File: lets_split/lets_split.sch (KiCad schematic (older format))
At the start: 60 parts, among them J1 3PIN, J2 6PIN, J3 3PIN, SW1 SW_PUSH, SW10 SW_PUSH, SW11 SW_PUSH, SW12 SW_PUSH, SW13 SW_PUSH, SW14 SW_PUSH, SW15 SW_PUSH, SW16 SW_PUSH, SW17 SW_PUSH, SW18 SW_PUSH, SW19 SW_PUSH, SW2 SW_PUSH, SW20 SW_PUSH, SW21 SW_PUSH, SW22 SW_PUSH, SW23 SW_PUSH, SW24 SW_PUSH, SW3 SW_PUSH, SW4 SW_PUSH, SW5 SW_PUSH, SW6 SW_PUSH, SW7 SW_PUSH, SW8 SW_PUSH, SW9 SW_PUSH, U1 TEENSY2.0, U2 HOLE, U3 HOLE, U4 HOLE, U5 HOLE

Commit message: Replace diode modules with SMD compatible one
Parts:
- D1, D10, D11, D12, D13, D14, D15, D16, D17, D18, D19, D2, D20, D21, D22, D23, D24, D3, D4, D5, D6, D7, D8, D9: footprint Diodes_ThroughHole:Diode_DO-41_SOD81_Horizontal_RM10 -> local:Diode_TH_SOD123
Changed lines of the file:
@@
 EESchema Schematic File Version 2
-LIBS:power
-LIBS:device
-LIBS:transistors
-LIBS:conn
-LIBS:linear
-LIBS:regul
-LIBS:74xx
-LIBS:cmos4000
-LIBS:adc-dac
-LIBS:memory
-LIBS:xilinx
-LIBS:microcontrollers
-LIBS:dsp
-LIBS:microchip
-LIBS:analog_switches
-LIBS:motorola
-LIBS:texas
-LIBS:intel
-LIBS:audio
-LIBS:interface
-LIBS:digital-audio
-LIBS:philips
-LIBS:display
-LIBS:cypress
-LIBS:siliconi
-LIBS:opto
-LIBS:atmel
-LIBS:contrib
-LIBS:valves
-LIBS:component
 LIBS:lets_split-cache
-EELAYER 25 0
+EELAYER 26 0
 EELAYER END
 $Descr A4 11693 8268
@@
 F 0 "D1" H 5750 2450 50  0000 C CNN
 F 1 "D" H 5750 2250 50  0000 C CNN
-F 2 "Diodes_ThroughHole:Diode_DO-41_SOD81_Horizontal_RM10" H 5750 2350 50  0001 C CNN
+F 2 "local:Diode_TH_SOD123" H 5750 2350 50  0001 C CNN
 F 3 "" H 5750 2350 50  0000 C CNN
 	1    5750 2350
@@
 F 0 "D5" H 6500 2450 50  0000 C CNN
 F 1 "D" H 6500 2250 50  0000 C CNN
-F 2 "Diodes_ThroughHole:Diode_DO-41_SOD81_Horizontal_RM10" H 6500 2350 50  0001 C CNN
+F 2 "local:Diode_TH_SOD123" H 6500 2350 50  0001 C CNN
 F 3 "" H 6500 2350 50  0000 C CNN
 	1    6500 2350
@@
 F 0 "D9" H 7200 2450 50  0000 C CNN
 F 1 "D" H 7200 2250 50  0000 C CNN
-F 2 "Diodes_ThroughHole:Diode_DO-41_SOD81_Horizontal_RM10" H 7200 2350 50  0001 C CNN
+F 2 "local:Diode_TH_SOD123" H 7200 2350 50  0001 C CNN
 F 3 "" H 7200 2350 50  0000 C CNN
 	1    7200 2350
@@
 F 0 "D13" H 7950 2450 50  0000 C CNN
 F 1 "D" H 7950 2250 50  0000 C CNN
-F 2 "Diodes_ThroughHole:Diode_DO-41_SOD81_Horizontal_RM10" H 7950 2350 50  0001 C CNN
+F 2 "local:Diode_TH_SOD123" H 7950 2350 50  0001 C CNN
 F 3 "" H 7950 2350 50  0000 C CNN
 	1    7950 2350
@@
 F 0 "D17" H 8700 2450 50  0000 C CNN
 F 1 "D" H 8700 2250 50  0000 C CNN
-F 2 "Diodes_ThroughHole:Diode_DO-41_SOD81_Horizontal_RM10" H 8700 2350 50  0001 C CNN
+F 2 "local:Diode_TH_SOD123" H 8700 2350 50  0001 C CNN
 F 3 "" H 8700 2350 50  0000 C CNN
 	1    8700 2350
@@
 F 0 "D21" H 9450 2450 50  0000 C CNN
 F 1 "D" H 9450 2250 50  0000 C CNN
-F 2 "Diodes_ThroughHole:Diode_DO-41_SOD81_Horizontal_RM10" H 9450 2350 50  0001 C CNN
+F 2 "local:Diode_TH_SOD123" H 9450 2350 50  0001 C CNN
 F 3 "" H 9450 2350 50  0000 C CNN
 	1    9450 2350
@@
 F 0 "D2" H 5750 2950 50  0000 C CNN
 F 1 "D" H 5750 2750 50  0000 C CNN
-F 2 "Diodes_ThroughHole:Diode_DO-41_SOD81_Horizontal_RM10" H 5750 2850 50  0001 C CNN
+F 2 "local:Diode_TH_SOD123" H 5750 2850 50  0001 C CNN
 F 3 "" H 5750 2850 50  0000 C CNN
 	1    5750 2850
@@
 F 0 "D6" H 6500 2950 50  0000 C CNN
 F 1 "D" H 6500 2750 50  0000 C CNN
-F 2 "Diodes_ThroughHole:Diode_DO-41_SOD81_Horizontal_RM10" H 6500 2850 50  0001 C CNN
+F 2 "local:Diode_TH_SOD123" H 6500 2850 50  0001 C CNN
 F 3 "" H 6500 2850 50  0000 C CNN
 	1    6500 2850
@@
 F 0 "D10" H 7200 2950 50  0000 C CNN
 F 1 "D" H 7200 2750 50  0000 C CNN
-F 2 "Diodes_ThroughHole:Diode_DO-41_SOD81_Horizontal_RM10" H 7200 2850 50  0001 C CNN
+F 2 "local:Diode_TH_SOD123" H 7200 2850 50  0001 C CNN
 F 3 "" H 7200 2850 50  0000 C CNN
 	1    7200 2850
@@
 F 0 "D14" H 7950 2950 50  0000 C CNN
 F 1 "D" H 7950 2750 50  0000 C CNN
-F 2 "Diodes_ThroughHole:Diode_DO-41_SOD81_Horizontal_RM10" H 7950 2850 50  0001 C CNN
+F 2 "local:Diode_TH_SOD123" H 7950 2850 50  0001 C CNN
 F 3 "" H 7950 2850 50  0000 C CNN
 	1    7950 2850
@@
 F 0 "D18" H 8700 2950 50  0000 C CNN
 F 1 "D" H 8700 2750 50  0000 C CNN
-F 2 "Diodes_ThroughHole:Diode_DO-41_SOD81_Horizontal_RM10" H 8700 2850 50  0001 C CNN
+F 2 "local:Diode_TH_SOD123" H 8700 2850 50  0001 C CNN
 F 3 "" H 8700 2850 50  0000 C CNN
 	1    8700 2850
@@
 F 0 "D22" H 9450 2950 50  0000 C CNN
 F 1 "D" H 9450 2750 50  0000 C CNN
-F 2 "Diodes_ThroughHole:Diode_DO-41_SOD81_Horizontal_RM10" H 9450 2850 50  0001 C CNN
+F 2 "local:Diode_TH_SOD123" H 9450 2850 50  0001 C CNN
 F 3 "" H 9450 2850 50  0000 C CNN
 	1    9450 2850
@@
 F 0 "D3" H 5750 3450 50  0000 C CNN
 F 1 "D" H 5750 3250 50  0000 C CNN
-F 2 "Diodes_ThroughHole:Diode_DO-41_SOD81_Horizontal_RM10" H 5750 3350 50  0001 C CNN
+F 2 "local:Diode_TH_SOD123" H 5750 3350 50  0001 C CNN
 F 3 "" H 5750 3350 50  0000 C CNN
 	1    5750 3350
@@
 F 0 "D7" H 6500 3450 50  0000 C CNN
 F 1 "D" H 6500 3250 50  0000 C CNN
-F 2 "Diodes_ThroughHole:Diode_DO-41_SOD81_Horizontal_RM10" H 6500 3350 50  0001 C CNN
+F 2 "local:Diode_TH_SOD123" H 6500 3350 50  0001 C CNN
 F 3 "" H 6500 3350 50  0000 C CNN
 	1    6500 3350
@@
 F 0 "D11" H 7200 3450 50  0000 C CNN
 F 1 "D" H 7200 3250 50  0000 C CNN
-F 2 "Diodes_ThroughHole:Diode_DO-41_SOD81_Horizontal_RM10" H 7200 3350 50  0001 C CNN
+F 2 "local:Diode_TH_SOD123" H 7200 3350 50  0001 C CNN
 F 3 "" H 7200 3350 50  0000 C CNN
 	1    7200 3350
@@
 F 0 "D15" H 7950 3450 50  0000 C CNN
 F 1 "D" H 7950 3250 50  0000 C CNN
-F 2 "Diodes_ThroughHole:Diode_DO-41_SOD81_Horizontal_RM10" H 7950 3350 50  0001 C CNN
+F 2 "local:Diode_TH_SOD123" H 7950 3350 50  0001 C CNN
 F 3 "" H 7950 3350 50  0000 C CNN
 	1    7950 3350
@@
 F 0 "D19" H 8700 3450 50  0000 C CNN
 F 1 "D" H 8700 3250 50  0000 C CNN
-F 2 "Diodes_ThroughHole:Diode_DO-41_SOD81_Horizontal_RM10" H 8700 3350 50  0001 C CNN
+F 2 "local:Diode_TH_SOD123" H 8700 3350 50  0001 C CNN
 F 3 "" H 8700 3350 50  0000 C CNN
 	1    8700 3350
@@
 F 0 "D23" H 9450 3450 50  0000 C CNN
 F 1 "D" H 9450 3250 50  0000 C CNN
-F 2 "Diodes_ThroughHole:Diode_DO-41_SOD81_Horizontal_RM10" H 9450 3350 50  0001 C CNN
+F 2 "local:Diode_TH_SOD123" H 9450 3350 50  0001 C CNN
 F 3 "" H 9450 3350 50  0000 C CNN
 	1    9450 3350
@@
 F 0 "D4" H 5750 3950 50  0000 C CNN
 F 1 "D" H 5750 3750 50  0000 C CNN
-F 2 "Diodes_ThroughHole:Diode_DO-41_SOD81_Horizontal_RM10" H 5750 3850 50  0001 C CNN
+F 2 "local:Diode_TH_SOD123" H 5750 3850 50  0001 C CNN
 F 3 "" H 5750 3850 50  0000 C CNN
 	1    5750 3850
@@
 F 0 "D8" H 6500 3950 50  0000 C CNN
 F 1 "D" H 6500 3750 50  0000 C CNN
-F 2 "Diodes_ThroughHole:Diode_DO-41_SOD81_Horizontal_RM10" H 6500 3850 50  0001 C CNN
+F 2 "local:Diode_TH_SOD123" H 6500 3850 50  0001 C CNN
 F 3 "" H 6500 3850 50  0000 C CNN
 	1    6500 3850
@@
 F 0 "D12" H 7200 3950 50  0000 C CNN
 F 1 "D" H 7200 3750 50  0000 C CNN
-F 2 "Diodes_ThroughHole:Diode_DO-41_SOD81_Horizontal_RM10" H 7200 3850 50  0001 C CNN
+F 2 "local:Diode_TH_SOD123" H 7200 3850 50  0001 C CNN
 F 3 "" H 7200 3850 50  0000 C CNN
 	1    7200 3850
@@
 F 0 "D16" H 7950 3950 50  0000 C CNN
 F 1 "D" H 7950 3750 50  0000 C CNN
-F 2 "Diodes_ThroughHole:Diode_DO-41_SOD81_Horizontal_RM10" H 7950 3850 50  0001 C CNN
+F 2 "local:Diode_TH_SOD123" H 7950 3850 50  0001 C CNN
 F 3 "" H 7950 3850 50  0000 C CNN
 	1    7950 3850
@@
 F 0 "D20" H 8700 3950 50  0000 C CNN
 F 1 "D" H 8700 3750 50  0000 C CNN
-F 2 "Diodes_ThroughHole:Diode_DO-41_SOD81_Horizontal_RM10" H 8700 3850 50  0001 C CNN
+F 2 "local:Diode_TH_SOD123" H 8700 3850 50  0001 C CNN
 F 3 "" H 8700 3850 50  0000 C CNN
 	1    8700 3850
@@
 F 0 "D24" H 9450 3950 50  0000 C CNN
 F 1 "D" H 9450 3750 50  0000 C CNN
-F 2 "Diodes_ThroughHole:Diode_DO-41_SOD81_Horizontal_RM10" H 9450 3850 50  0001 C CNN
+F 2 "local:Diode_TH_SOD123" H 9450 3850 50  0001 C CNN
 F 3 "" H 9450 3850 50  0000 C CNN
 	1    9450 3850

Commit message: Replace resistor footprint with one having silk on both sides
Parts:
- R1, R2: footprint footprint:RESISTOR -> local:RESISTOR
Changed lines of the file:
@@
 F 0 "R2" V 6380 950 50  0000 C CNN
 F 1 "R" V 6300 950 50  0000 C CNN
-F 2 "footprint:RESISTOR" V 6230 950 50  0001 C CNN
+F 2 "local:RESISTOR" V 6230 950 50  0001 C CNN
 F 3 "" H 6300 950 50  0000 C CNN
 	1    6300 950
@@
 F 0 "R1" V 4680 750 50  0000 C CNN
 F 1 "R" V 4600 750 50  0000 C CNN
-F 2 "footprint:RESISTOR" V 4530 750 50  0001 C CNN
+F 2 "local:RESISTOR" V 4530 750 50  0001 C CNN
 F 3 "" H 4600 750 50  0000 C CNN
 	1    4600 750

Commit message: Replace Teensy 2.0 symbol with Pro Micro one
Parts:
- removed U1: TEENSY2.0, footprint:TEENSY_2.0, symbol TEENSY2.0
- added U1: ProMicro, local:ProMicro, symbol ProMicro
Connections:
- wire segments 24 -> 31
- no-connect marks 0 -> 8
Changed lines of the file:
@@
 EESchema Schematic File Version 2
+LIBS:promicro
 LIBS:lets_split-cache
 EELAYER 26 0
@@
 Connection ~ 8850 3200
 $Comp
-L TEENSY2.0 U1
-U 1 1 57D48AE5
-P 2000 2950
-F 0 "U1" V 2050 2950 60  0000 C CNN
-F 1 "TEENSY2.0" V 1950 2950 60  0000 C CNN
-F 2 "footprint:TEENSY_2.0" H 2000 2950 60  0001 C CNN
-F 3 "" H 2000 2950 60  0000 C CNN
-	1    2000 2950
-	1    0    0    -1
-$EndComp
-$Comp
 L 6PIN J2
 U 1 1 57D49FBD
@@
 Wire Wire Line
 	6400 1150 6400 1450
-Text GLabel 2600 4150 2    60   Input ~ 0
-data
 Text GLabel 6450 950  1    60   Input ~ 0
 data
@@
 	1    4600 600
 	0    1    1    0
-$EndComp
-Wire Wire Line
-	4600 900  4600 4050
-Wire Wire Line
-	4600 4050 2600 4050
-Text GLabel 2600 2750 2    60   Input ~ 0
-col0
-Text GLabel 2600 2850 2    60   Input ~ 0
-col1
-Text GLabel 2600 2950 2    60   Input ~ 0
-col2
-Text GLabel 2600 3050 2    60   Input ~ 0
-col3
-Text GLabel 2600 2500 2    60   Input ~ 0
-col4
-Text GLabel 2600 2600 2    60   Input ~ 0
-col5
-Text GLabel 2600 3350 2    60   Input ~ 0
-row3
-Text GLabel 2600 3450 2    60   Input ~ 0
-row2
-Text GLabel 2600 2050 2    60   Input ~ 0
-row1
-Text GLabel 2600 2150 2    60   Input ~ 0
-row0
-$Comp
-L VCC #PWR07
-U 1 1 57D5E2B3
-P 2600 1850
-F 0 "#PWR07" H 2600 1700 50  0001 C CNN
-F 1 "VCC" H 2600 2000 50  0000 C CNN
-F 2 "" H 2600 1850 50  0000 C CNN
-F 3 "" H 2600 1850 50  0000 C CNN
-	1    2600 1850
-	0    1    1    0
-$EndComp
-$Comp
-L GND #PWR08
-U 1 1 57D5FCCF
-P 2600 1650
-F 0 "#PWR08" H 2600 1400 50  0001 C CNN
-F 1 "GND" H 2600 1500 50  0000 C CNN
-F 2 "" H 2600 1650 50  0000 C CNN
-F 3 "" H 2600 1650 50  0000 C CNN
-	1    2600 1650
-	0    -1   -1   0
-$EndComp
-$Comp
-L GND #PWR09
-U 1 1 57D5FDD2
-P 2600 3850
-F 0 "#PWR09" H 2600 3600 50  0001 C CNN
-F 1 "GND" H 2600 3700 50  0000 C CNN
-F 2 "" H 2600 3850 50  0000 C CNN
-F 3 "" H 2600 3850 50  0000 C CNN
-	1    2600 3850
-	0    -1   -1   0
-$EndComp
-$Comp
-L GND #PWR010
-U 1 1 57D5FE56
-P 2600 3950
-F 0 "#PWR010" H 2600 3700 50  0001 C CNN
-F 1 "GND" H 2600 3800 50  0000 C CNN
-F 2 "" H 2600 3950 50  0000 C CNN
-F 3 "" H 2600 3950 50  0000 C CNN
-	1    2600 3950
-	0    -1   -1   0
 $EndComp
 Text GLabel 5150 2200 1    60   Input ~ 0
@@
 	1    0    0    -1
 $EndComp
+$Comp
+L ProMicro U1
+U 1 1 59A40F45
+P 2850 3150
+F 0 "U1" H 2550 3850 60  0000 C CNN
+F 1 "ProMicro" H 2850 2450 60  0000 C CNN
+F 2 "local:ProMicro" H 2950 2900 60  0001 C CNN
+F 3 "" H 2950 2900 60  0000 C CNN
+	1    2850 3150
+	1    0    0    -1
+$EndComp
+$Comp
+L GND #PWR?
+U 1 1 59A417D7
+P 3500 2700
+F 0 "#PWR?" H 3500 2450 50  0001 C CNN
+F 1 "GND" H 3500 2550 50  0000 C CNN
+F 2 "" H 3500 2700 50  0000 C CNN
+F 3 "" H 3500 2700 50  0000 C CNN
+	1    3500 2700
+	0    -1   -1   0
+$EndComp
+Wire Wire Line
+	3500 2700 3400 2700
+$Comp
+L VCC #PWR?
+U 1 1 59A41DD4
+P 3500 2900
+F 0 "#PWR?" H 3500 2750 50  0001 C CNN
+F 1 "VCC" H 3500 3050 50  0000 C CNN
+F 2 "" H 3500 2900 50  0000 C CNN
+F 3 "" H 3500 2900 50  0000 C CNN
+	1    3500 2900
+	0    1    1    0
+$EndComp
+Wire Wire Line
+	3400 2900 3500 2900
+Text GLabel 2300 3500 0    60   Input ~ 0
+row1
+Text GLabel 2300 3400 0    60   Input ~ 0
+row0
+Text GLabel 2300 3600 0    60   Input ~ 0
+row2
+Text GLabel 2300 3700 0    60   Input ~ 0
+row3
+Text GLabel 3400 3200 2    60   Input ~ 0
+col0
+Text GLabel 3400 3300 2    60   Input ~ 0
+col1
+Text GLabel 3400 3400 2    60   Input ~ 0
+col2
+Text GLabel 3400 3500 2    60   Input ~ 0
+col3
+Text GLabel 3400 3600 2    60   Input ~ 0
+col4
+Text GLabel 3400 3700 2    60   Input ~ 0
+col5
+$Comp
+L GND #PWR?
+U 1 1 59A45F78
+P 2200 2800
+F 0 "#PWR?" H 2200 2550 50  0001 C CNN
+F 1 "GND" H 2200 2650 50  0000 C CNN
+F 2 "" H 2200 2800 50  0000 C CNN
+F 3 "" H 2200 2800 50  0000 C CNN
+	1    2200 2800
+	0    1    1    0
+$EndComp
+Wire Wire Line
+	2300 2800 2200 2800
+Wire Wire Line
+	2300 2900 2250 2900
+Wire Wire Line
+	2250 2900 2250 2800
+Connection ~ 2250 2800
+Text GLabel 2300 3100 0    60   Input ~ 0
+data
+NoConn ~ 2300 2600
+NoConn ~ 2300 2700
+NoConn ~ 2300 3200
+NoConn ~ 2300 3300
+NoConn ~ 3400 2600
+NoConn ~ 3400 2800
+NoConn ~ 3400 3000
+NoConn ~ 3400 3100
+Wire Wire Line
+	1900 3000 2300 3000
+Wire Wire Line
+	4600 900  4600 1750
+Wire Wire Line
+	4600 1750 1900 1750
+Wire Wire Line
+	1900 1750 1900 3000
 $EndSCHEMATC

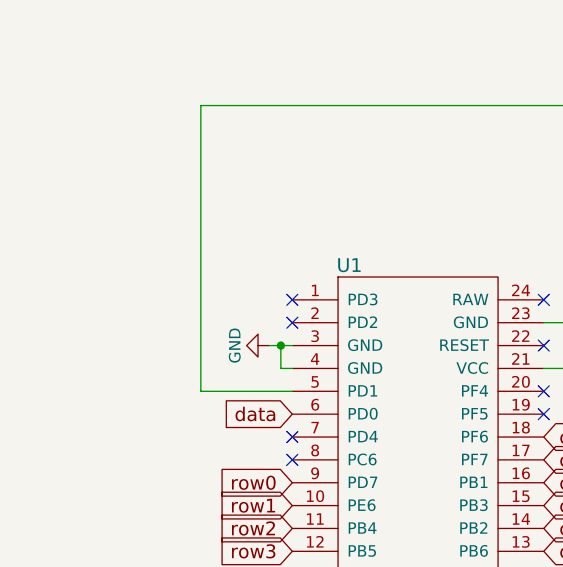
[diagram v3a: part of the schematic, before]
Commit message: Add IO pad for RGB underglow
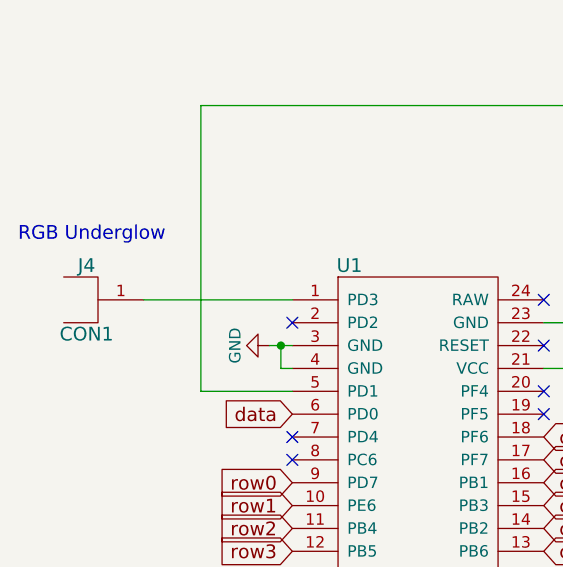
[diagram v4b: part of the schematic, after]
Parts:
- added J4: CON1, local:CON1, symbol CON1
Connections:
- net at U1.1 (PD3): now also J4.1
- no-connect marks 8 -> 7
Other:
- note added: "RGB Underglow"
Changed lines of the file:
@@
 EESchema Schematic File Version 2
 LIBS:promicro
+LIBS:local
 LIBS:lets_split-cache
 EELAYER 26 0
@@
 $EndComp
 $Comp
-L GND #PWR?
+L GND #PWR07
 U 1 1 59A417D7
 P 3500 2700
-F 0 "#PWR?" H 3500 2450 50  0001 C CNN
+F 0 "#PWR07" H 3500 2450 50  0001 C CNN
 F 1 "GND" H 3500 2550 50  0000 C CNN
 F 2 "" H 3500 2700 50  0000 C CNN
@@
 	3500 2700 3400 2700
 $Comp
-L VCC #PWR?
+L VCC #PWR09
 U 1 1 59A41DD4
 P 3500 2900
-F 0 "#PWR?" H 3500 2750 50  0001 C CNN
+F 0 "#PWR09" H 3500 2750 50  0001 C CNN
 F 1 "VCC" H 3500 3050 50  0000 C CNN
 F 2 "" H 3500 2900 50  0000 C CNN
@@
 col5
 $Comp
-L GND #PWR?
+L GND #PWR08
 U 1 1 59A45F78
 P 2200 2800
-F 0 "#PWR?" H 2200 2550 50  0001 C CNN
+F 0 "#PWR08" H 2200 2550 50  0001 C CNN
 F 1 "GND" H 2200 2650 50  0000 C CNN
 F 2 "" H 2200 2800 50  0000 C CNN
@@
 Text GLabel 2300 3100 0    60   Input ~ 0
 data
-NoConn ~ 2300 2600
 NoConn ~ 2300 2700
 NoConn ~ 2300 3200
@@
 Wire Wire Line
 	1900 1750 1900 3000
+$Comp
+L CON1 J4
+U 1 1 59A446B6
+P 1400 2600
+F 0 "J4" H 1400 2750 60  0000 C CNN
+F 1 "CON1" H 1400 2450 60  0000 C CNN
+F 2 "local:CON1" H 1350 2600 60  0001 C CNN
+F 3 "" H 1350 2600 60  0001 C CNN
+	1    1400 2600
+	1    0    0    -1
+$EndComp
+Wire Wire Line
+	2300 2600 1650 2600
+Text Notes 1100 2350 0    60   ~ 0
+RGB Underglow
 $EndSCHEMATC

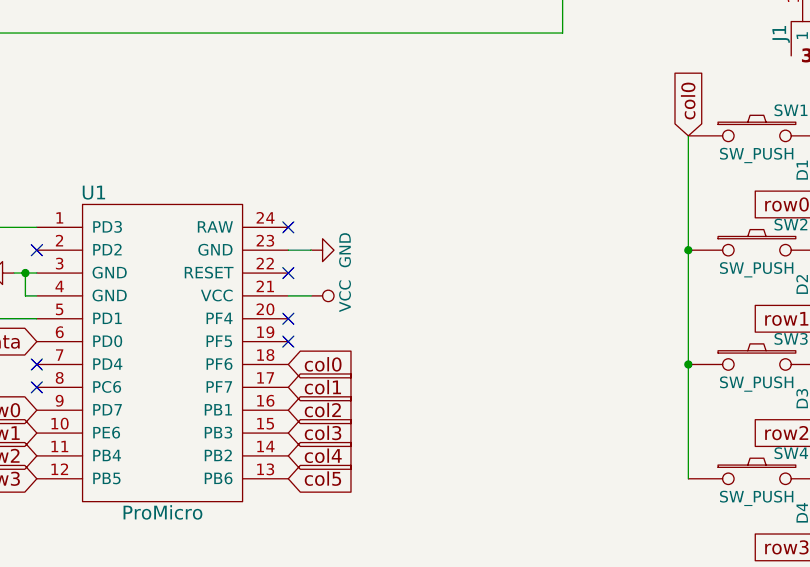
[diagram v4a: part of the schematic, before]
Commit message: Add reset switch, changes outer shape of the board
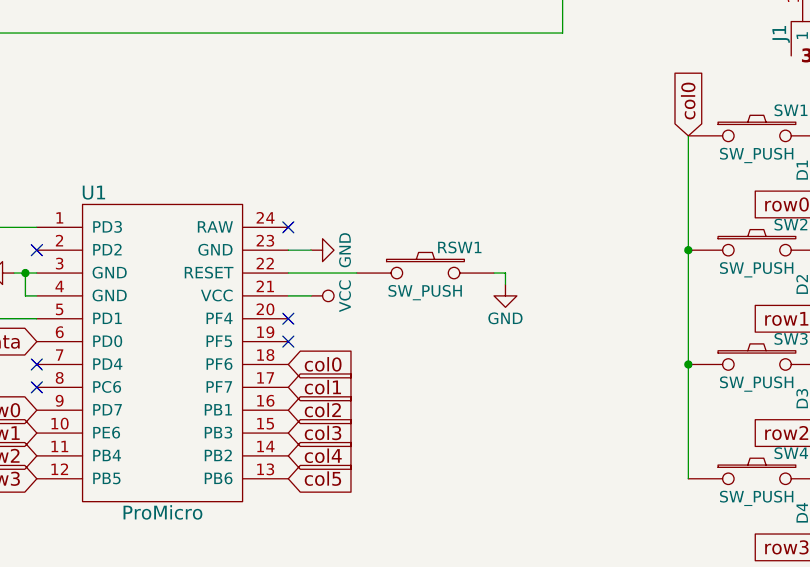
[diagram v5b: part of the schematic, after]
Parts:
- added RSW1: SW_PUSH, local:SKHL, symbol SW_PUSH
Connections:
- net GND: now also RSW1.2
- net at U1.22 (RESET): now also RSW1.1
- no-connect marks 7 -> 6
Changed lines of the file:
@@
 NoConn ~ 2300 3300
 NoConn ~ 3400 2600
-NoConn ~ 3400 2800
 NoConn ~ 3400 3000
 NoConn ~ 3400 3100
@@
 Text Notes 1100 2350 0    60   ~ 0
 RGB Underglow
+$Comp
+L SW_PUSH RSW1
+U 1 1 59A4BD25
+P 4000 2800
+F 0 "RSW1" H 4150 2910 50  0000 C CNN
+F 1 "SW_PUSH" H 4000 2720 50  0000 C CNN
+F 2 "local:SKHL" H 4000 2800 50  0001 C CNN
+F 3 "" H 4000 2800 50  0000 C CNN
+	1    4000 2800
+	1    0    0    -1
+$EndComp
+$Comp
+L GND #PWR010
+U 1 1 59A4C0CB
+P 4350 2850
+F 0 "#PWR010" H 4350 2600 50  0001 C CNN
+F 1 "GND" H 4350 2700 50  0000 C CNN
+F 2 "" H 4350 2850 50  0000 C CNN
+F 3 "" H 4350 2850 50  0000 C CNN
+	1    4350 2850
+	1    0    0    -1
+$EndComp
+Wire Wire Line
+	4350 2850 4350 2800
+Wire Wire Line
+	4350 2800 4300 2800
+Wire Wire Line
+	3700 2800 3400 2800
 $EndSCHEMATC

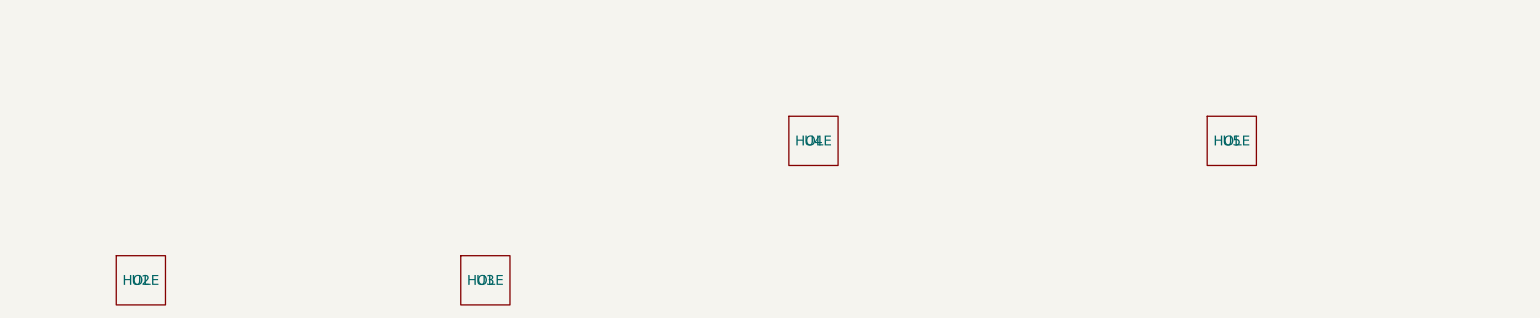
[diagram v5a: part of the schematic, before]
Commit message: Use smaller hole symbol
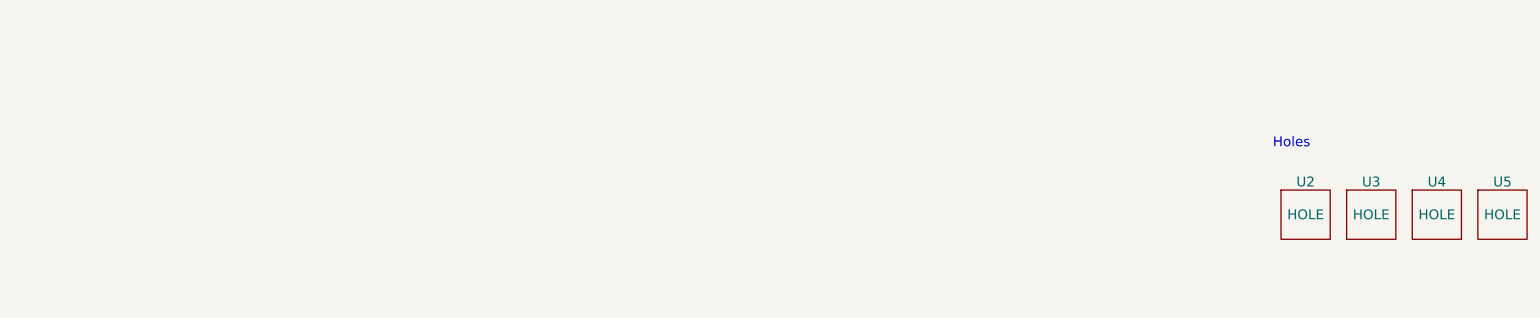
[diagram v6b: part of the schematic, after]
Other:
- note added: "Holes"
- moved on the sheet: U2, U3, U4, U5
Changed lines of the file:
@@
 L HOLE U2
 U 1 1 57D4E136
-P 1950 6500
-F 0 "U2" H 1950 6500 60  0000 C CNN
-F 1 "HOLE" H 1950 6500 60  0000 C CNN
-F 2 "prettylib:HOLE" H 1950 6500 60  0001 C CNN
-F 3 "" H 1950 6500 60  0000 C CNN
-	1    1950 6500
+P 9050 6100
+F 0 "U2" H 9050 6300 60  0000 C CNN
+F 1 "HOLE" H 9050 6100 60  0000 C CNN
+F 2 "prettylib:HOLE" H 9050 6100 60  0001 C CNN
+F 3 "" H 9050 6100 60  0000 C CNN
+	1    9050 6100
 	1    0    0    -1
 $EndComp
@@
 L HOLE U3
 U 1 1 57D4E261
-P 4050 6500
-F 0 "U3" H 4050 6500 60  0000 C CNN
-F 1 "HOLE" H 4050 6500 60  0000 C CNN
-F 2 "prettylib:HOLE" H 4050 6500 60  0001 C CNN
-F 3 "" H 4050 6500 60  0000 C CNN
-	1    4050 6500
+P 9450 6100
+F 0 "U3" H 9450 6300 60  0000 C CNN
+F 1 "HOLE" H 9450 6100 60  0000 C CNN
+F 2 "prettylib:HOLE" H 9450 6100 60  0001 C CNN
+F 3 "" H 9450 6100 60  0000 C CNN
+	1    9450 6100
 	1    0    0    -1
 $EndComp
@@
 L HOLE U4
 U 1 1 57D4E2F6
-P 6050 5650
-F 0 "U4" H 6050 5650 60  0000 C CNN
-F 1 "HOLE" H 6050 5650 60  0000 C CNN
-F 2 "prettylib:HOLE" H 6050 5650 60  0001 C CNN
-F 3 "" H 6050 5650 60  0000 C CNN
-	1    6050 5650
+P 9850 6100
+F 0 "U4" H 9850 6300 60  0000 C CNN
+F 1 "HOLE" H 9850 6100 60  0000 C CNN
+F 2 "prettylib:HOLE" H 9850 6100 60  0001 C CNN
+F 3 "" H 9850 6100 60  0000 C CNN
+	1    9850 6100
 	1    0    0    -1
 $EndComp
@@
 L HOLE U5
 U 1 1 57D4E38F
-P 8600 5650
-F 0 "U5" H 8600 5650 60  0000 C CNN
-F 1 "HOLE" H 8600 5650 60  0000 C CNN
-F 2 "prettylib:HOLE" H 8600 5650 60  0001 C CNN
-F 3 "" H 8600 5650 60  0000 C CNN
-	1    8600 5650
+P 10250 6100
+F 0 "U5" H 10250 6300 60  0000 C CNN
+F 1 "HOLE" H 10250 6100 60  0000 C CNN
+F 2 "prettylib:HOLE" H 10250 6100 60  0001 C CNN
+F 3 "" H 10250 6100 60  0000 C CNN
+	1    10250 6100
 	1    0    0    -1
 $EndComp
@@
 Wire Wire Line
 	3700 2800 3400 2800
+Text Notes 8850 5700 0    60   ~ 0
+Holes
 $EndSCHEMATC
